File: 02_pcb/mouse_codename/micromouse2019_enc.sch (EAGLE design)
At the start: 7 parts, among them IC1 AS5047D

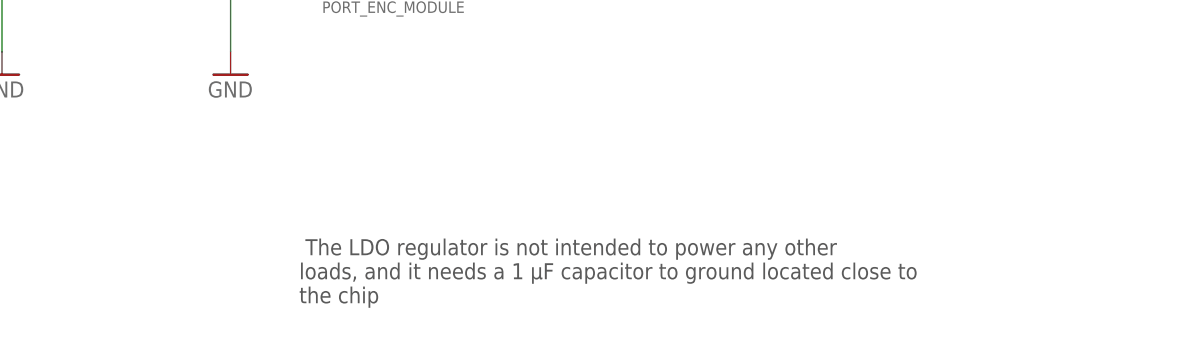
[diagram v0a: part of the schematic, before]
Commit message: BT_PORT_BASE updated
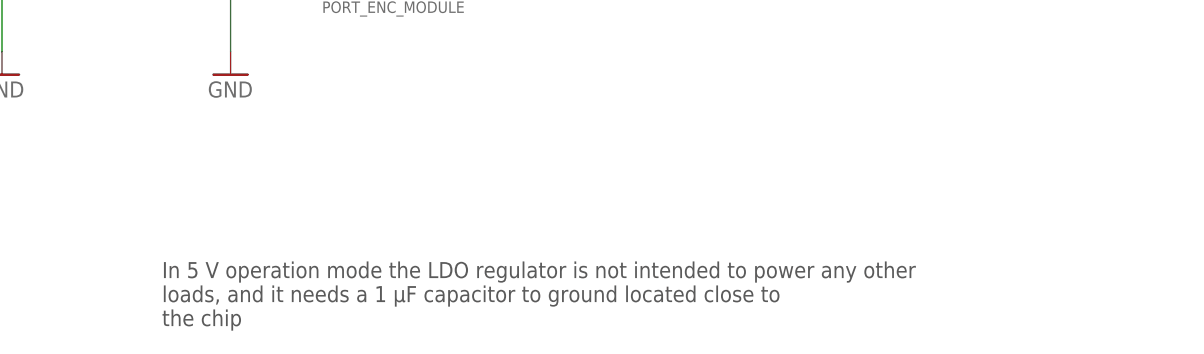
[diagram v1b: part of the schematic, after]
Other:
- note added: "In 5 V operation mode the LDO regulator is not intended to power any other loads, and it needs a 1 μF capacitor to ground located close to the chip"
- note removed: "The LDO regulator is not intended to power any other loads, and it needs a 1 μF capacitor to ground located close to the chip"
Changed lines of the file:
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@@
 <sheet>
 <plain>
-<text x="182.88" y="58.42" size="1.778" layer="97"> The LDO regulator is not intended to power any other
+<text x="167.64" y="55.88" size="1.778" layer="97">In 5 V operation mode the LDO regulator is not intended to power any other
 loads, and it needs a 1 μF capacitor to ground located close to
 the chip</text>
